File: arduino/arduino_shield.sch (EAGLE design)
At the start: 14 parts, among them IC3 PCF8574T, IC4 PCF8574T

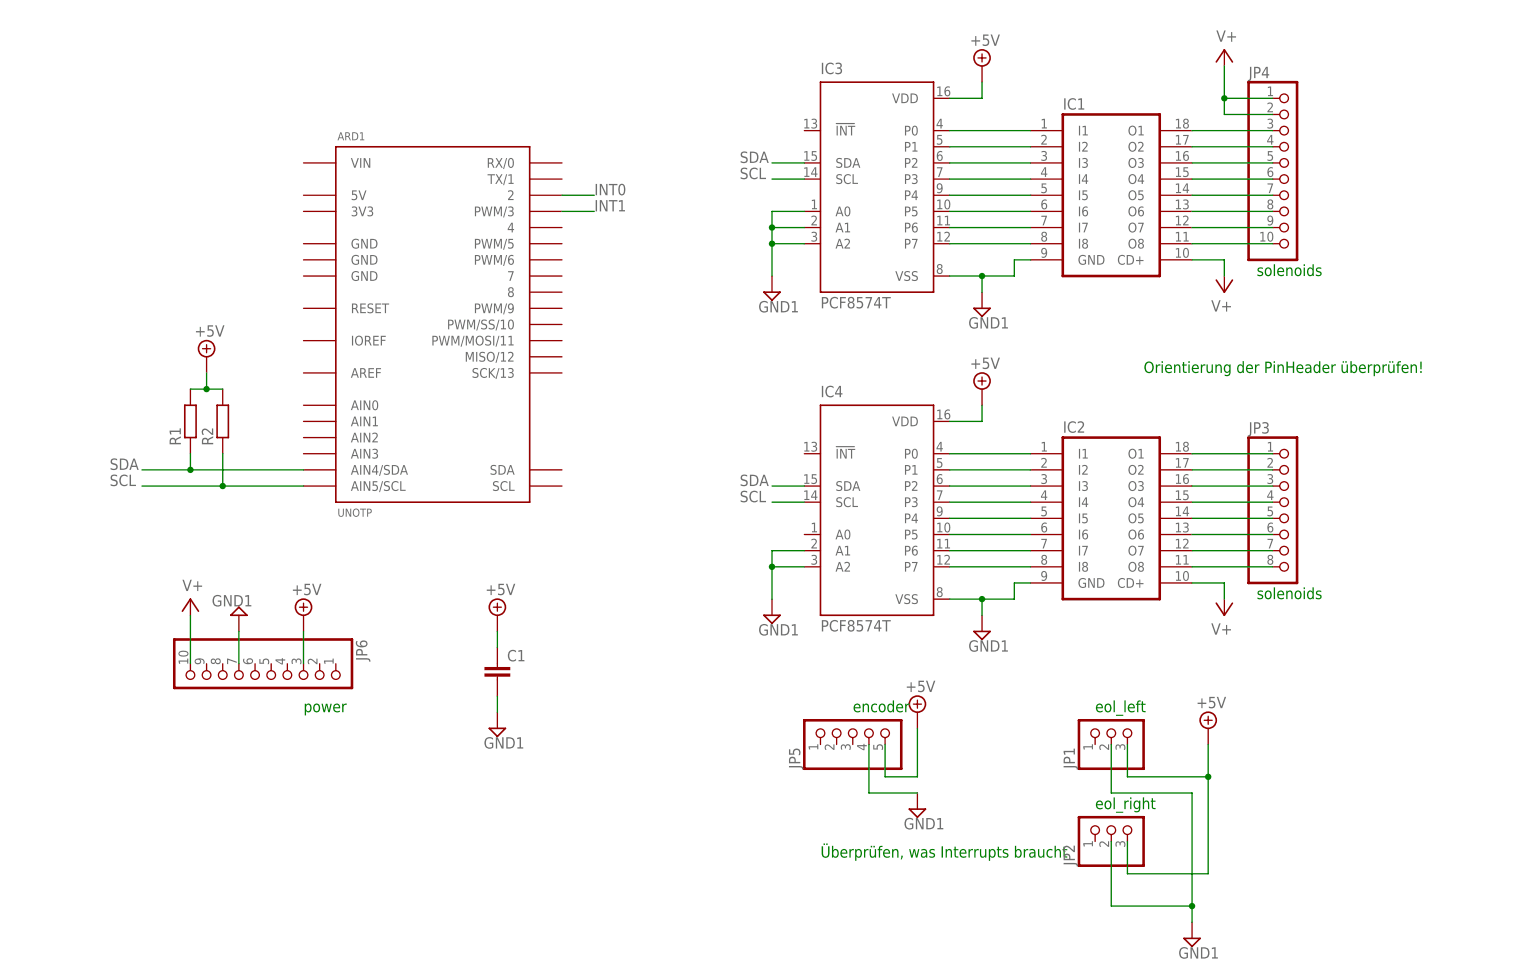
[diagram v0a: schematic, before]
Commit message: Wired EOLs and ENCODER to Arduino, added Buzzer and Supplyvoltage Jumper
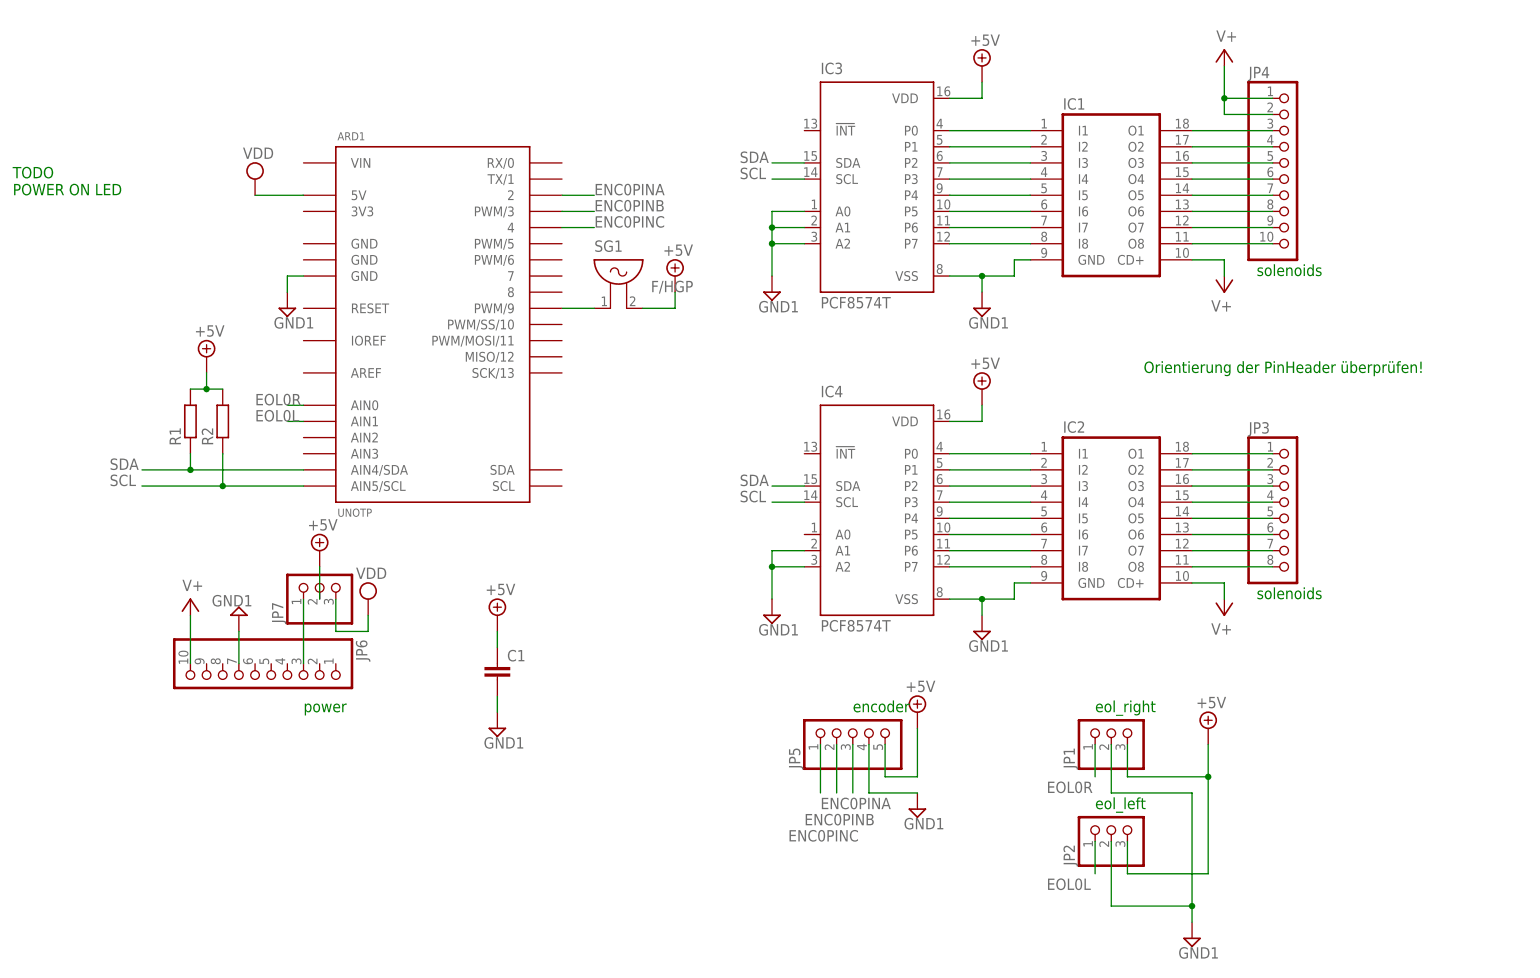
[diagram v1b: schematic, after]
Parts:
- added JP7: (no value), pinhead:PINHD-1X3
- added SG1: F/HGP, buzzer:F/HGP
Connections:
- removed net INT0: ARD1.2
- removed net INT1: ARD1.PWM/3
- new net ENC0PINA: ARD1.2, JP5.3
- new net ENC0PINB: ARD1.PWM/3, JP5.2
- new net ENC0PINC: ARD1.4, JP5.1
- new net EOL0L: ARD1.AIN1, JP2.1
- new net EOL0R: ARD1.AIN0, JP1.1
- new net N$33: JP6.3, JP7.1
- new net N$34: ARD1.PWM/9, SG1.1
- new net VDD: ARD1.5V, JP7.3
- net +5V: now also JP7.2, SG1.2; no longer JP6.3
- net GND1: now also ARD1.GND@3
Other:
- note added: "TODO POWER ON LED"
- note removed: "Überprüfen, was Interrupts braucht"
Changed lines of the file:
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@@
 <part name="SUPPLY13" library="supply2" deviceset="V+" device=""/>
 <part name="SUPPLY14" library="supply2" deviceset="GND1" device=""/>
-<part name="SUPPLY15" library="supply2" deviceset="+5V" device=""/>
 <part name="SUPPLY16" library="supply2" deviceset="+5V" device=""/>
 <part name="SUPPLY17" library="supply2" deviceset="GND1" device=""/>
 <part name="SUPPLY18" library="supply2" deviceset="GND1" device=""/>
 <part name="SUPPLY19" library="supply2" deviceset="+5V" device=""/>
+<part name="SUPPLY20" library="supply2" deviceset="GND1" device=""/>
+<part name="SG1" library="buzzer" deviceset="F/HGP" device=""/>
+<part name="SUPPLY21" library="supply2" deviceset="+5V" device=""/>
+<part name="JP7" library="pinhead" deviceset="PINHD-1X3" device=""/>
+<part name="SUPPLY15" library="supply2" deviceset="+5V" device=""/>
+<part name="SUPPLY22" library="supply2" deviceset="VDD" device=""/>
+<part name="SUPPLY23" library="supply2" deviceset="VDD" device=""/>
 </parts>
 <sheets>
 <sheet>
 <plain>
-<text x="25.4" y="-35.56" size="1.778" layer="91">eol_left</text>
-<text x="25.4" y="-50.8" size="1.778" layer="91">eol_right</text>
+<text x="25.4" y="-50.8" size="1.778" layer="91">eol_left</text>
+<text x="25.4" y="-35.56" size="1.778" layer="91">eol_right</text>
 <text x="-12.7" y="-35.56" size="1.778" layer="91">encoder</text>
 <text x="50.8" y="33.02" size="1.778" layer="91">solenoids</text>
@@
 <text x="-99.06" y="-35.56" size="1.778" layer="91">power</text>
 <text x="33.02" y="17.78" size="1.778" layer="91">Orientierung der PinHeader überprüfen!</text>
-<text x="-17.78" y="-58.42" size="1.778" layer="91">Überprüfen, was Interrupts braucht</text>
+<text x="-144.78" y="45.72" size="1.778" layer="91">TODO
+POWER ON LED</text>
 </plain>
 <instances>
@@
 <instance part="SUPPLY13" gate="1" x="-116.84" y="-17.78"/>
 <instance part="SUPPLY14" gate="G$1" x="-109.22" y="-20.32" rot="R180"/>
-<instance part="SUPPLY15" gate="+5V" x="-99.06" y="-20.32"/>
 <instance part="SUPPLY16" gate="+5V" x="43.18" y="-38.1"/>
 <instance part="SUPPLY17" gate="G$1" x="40.64" y="-71.12"/>
 <instance part="SUPPLY18" gate="G$1" x="-2.54" y="-50.8"/>
 <instance part="SUPPLY19" gate="+5V" x="-2.54" y="-35.56"/>
+<instance part="SUPPLY20" gate="G$1" x="-101.6" y="27.94"/>
+<instance part="SG1" gate="G$1" x="-50.8" y="30.48"/>
+<instance part="SUPPLY21" gate="+5V" x="-40.64" y="33.02"/>
+<instance part="JP7" gate="A" x="-96.52" y="-15.24" rot="R90"/>
+<instance part="SUPPLY15" gate="+5V" x="-96.52" y="-10.16"/>
+<instance part="SUPPLY22" gate="G$1" x="-106.68" y="48.26"/>
+<instance part="SUPPLY23" gate="G$1" x="-88.9" y="-17.78"/>
 </instances>
 <busses>
@@
 <wire x1="2.54" y1="10.16" x2="7.62" y2="10.16" width="0.1524" layer="91"/>
 <wire x1="7.62" y1="10.16" x2="7.62" y2="12.7" width="0.1524" layer="91"/>
-</segment>
-<segment>
-<pinref part="JP6" gate="A" pin="3"/>
-<pinref part="SUPPLY15" gate="+5V" pin="+5V"/>
-<wire x1="-99.06" y1="-27.94" x2="-99.06" y2="-22.86" width="0.1524" layer="91"/>
 </segment>
 <segment>
@@
 <wire x1="-7.62" y1="-45.72" x2="-2.54" y2="-45.72" width="0.1524" layer="91"/>
 <wire x1="-2.54" y1="-45.72" x2="-2.54" y2="-38.1" width="0.1524" layer="91"/>
+</segment>
+<segment>
+<pinref part="SG1" gate="G$1" pin="2"/>
+<wire x1="-45.72" y1="27.94" x2="-40.64" y2="27.94" width="0.1524" layer="91"/>
+<wire x1="-40.64" y1="27.94" x2="-40.64" y2="30.48" width="0.1524" layer="91"/>
+<pinref part="SUPPLY21" gate="+5V" pin="+5V"/>
+</segment>
+<segment>
+<pinref part="JP7" gate="A" pin="2"/>
+<pinref part="SUPPLY15" gate="+5V" pin="+5V"/>
+<wire x1="-96.52" y1="-17.78" x2="-96.52" y2="-12.7" width="0.1524" layer="91"/>
 </segment>
 </net>
@@
 <wire x1="-10.16" y1="-48.26" x2="-2.54" y2="-48.26" width="0.1524" layer="91"/>
 </segment>
+<segment>
+<pinref part="ARD1" gate="G$1" pin="GND@3"/>
+<wire x1="-99.06" y1="33.02" x2="-101.6" y2="33.02" width="0.1524" layer="91"/>
+<wire x1="-101.6" y1="33.02" x2="-101.6" y2="30.48" width="0.1524" layer="91"/>
+<pinref part="SUPPLY20" gate="G$1" pin="GND1"/>
+</segment>
 </net>
 <net name="N$2" class="0">
@@
 <junction x="-111.76" y="0"/>
 <label x="-129.54" y="0" size="1.778" layer="95"/>
-</segment>
-</net>
-<net name="INT0" class="0">
-<segment>
-<pinref part="ARD1" gate="G$1" pin="2"/>
-<wire x1="-58.42" y1="45.72" x2="-53.34" y2="45.72" width="0.1524" layer="91"/>
-<label x="-53.34" y="45.72" size="1.778" layer="95"/>
-</segment>
-</net>
-<net name="INT1" class="0">
-<segment>
-<pinref part="ARD1" gate="G$1" pin="PWM/3"/>
-<wire x1="-58.42" y1="43.18" x2="-53.34" y2="43.18" width="0.1524" layer="91"/>
-<label x="-53.34" y="43.18" size="1.778" layer="95"/>
 </segment>
 </net>
@@
 </segment>
 </net>
+<net name="ENC0PINA" class="0">
+<segment>
+<pinref part="JP5" gate="A" pin="3"/>
+<wire x1="-12.7" y1="-40.64" x2="-12.7" y2="-48.26" width="0.1524" layer="91"/>
+<label x="-17.78" y="-50.8" size="1.778" layer="95"/>
+</segment>
+<segment>
+<pinref part="ARD1" gate="G$1" pin="2"/>
+<wire x1="-58.42" y1="45.72" x2="-53.34" y2="45.72" width="0.1524" layer="91"/>
+<label x="-53.34" y="45.72" size="1.778" layer="95"/>
+</segment>
+</net>
+<net name="ENC0PINB" class="0">
+<segment>
+<pinref part="JP5" gate="A" pin="2"/>
+<wire x1="-15.24" y1="-40.64" x2="-15.24" y2="-48.26" width="0.1524" layer="91"/>
+<label x="-20.32" y="-53.34" size="1.778" layer="95"/>
+</segment>
+<segment>
+<pinref part="ARD1" gate="G$1" pin="PWM/3"/>
+<wire x1="-58.42" y1="43.18" x2="-53.34" y2="43.18" width="0.1524" layer="91"/>
+<label x="-53.34" y="43.18" size="1.778" layer="95"/>
+</segment>
+</net>
+<net name="ENC0PINC" class="0">
+<segment>
+<pinref part="JP5" gate="A" pin="1"/>
+<wire x1="-17.78" y1="-40.64" x2="-17.78" y2="-48.26" width="0.1524" layer="91"/>
+<label x="-22.86" y="-55.88" size="1.778" layer="95"/>
+</segment>
+<segment>
+<pinref part="ARD1" gate="G$1" pin="4"/>
+<wire x1="-58.42" y1="40.64" x2="-53.34" y2="40.64" width="0.1524" layer="91"/>
+<label x="-53.34" y="40.64" size="1.778" layer="95"/>
+</segment>
+</net>
+<net name="EOL0R" class="0">
+<segment>
+<pinref part="JP1" gate="A" pin="1"/>
+<wire x1="25.4" y1="-40.64" x2="25.4" y2="-45.72" width="0.1524" layer="91"/>
+<label x="17.78" y="-48.26" size="1.778" layer="95"/>
+</segment>
+<segment>
+<pinref part="ARD1" gate="G$1" pin="AIN0"/>
+<wire x1="-99.06" y1="12.7" x2="-101.6" y2="12.7" width="0.1524" layer="91"/>
+<label x="-106.68" y="12.7" size="1.778" layer="95"/>
+</segment>
+</net>
+<net name="EOL0L" class="0">
+<segment>
+<pinref part="JP2" gate="A" pin="1"/>
+<wire x1="25.4" y1="-55.88" x2="25.4" y2="-60.96" width="0.1524" layer="91"/>
+<label x="17.78" y="-63.5" size="1.778" layer="95"/>
+</segment>
+<segment>
+<pinref part="ARD1" gate="G$1" pin="AIN1"/>
+<wire x1="-99.06" y1="10.16" x2="-101.6" y2="10.16" width="0.1524" layer="91"/>
+<label x="-106.68" y="10.16" size="1.778" layer="95"/>
+</segment>
+</net>
+<net name="N$34" class="0">
+<segment>
+<pinref part="ARD1" gate="G$1" pin="PWM/9"/>
+<pinref part="SG1" gate="G$1" pin="1"/>
+<wire x1="-58.42" y1="27.94" x2="-53.34" y2="27.94" width="0.1524" layer="91"/>
+</segment>
+</net>
+<net name="N$33" class="0">
+<segment>
+<pinref part="JP6" gate="A" pin="3"/>
+<pinref part="JP7" gate="A" pin="1"/>
+<wire x1="-99.06" y1="-27.94" x2="-99.06" y2="-17.78" width="0.1524" layer="91"/>
+</segment>
+</net>
+<net name="VDD" class="0">
+<segment>
+<pinref part="ARD1" gate="G$1" pin="5V"/>
+<pinref part="SUPPLY22" gate="G$1" pin="VDD"/>
+<wire x1="-99.06" y1="45.72" x2="-106.68" y2="45.72" width="0.1524" layer="91"/>
+</segment>
+<segment>
+<pinref part="JP7" gate="A" pin="3"/>
+<wire x1="-93.98" y1="-17.78" x2="-93.98" y2="-22.86" width="0.1524" layer="91"/>
+<pinref part="SUPPLY23" gate="G$1" pin="VDD"/>
+<wire x1="-93.98" y1="-22.86" x2="-88.9" y2="-22.86" width="0.1524" layer="91"/>
+<wire x1="-88.9" y1="-22.86" x2="-88.9" y2="-20.32" width="0.1524" layer="91"/>
+</segment>
+</net>
 </nets>
 </sheet>
@@
 </schematic>
 </drawing>
+<compatibility>
+<note version="6.3" minversion="6.2.2" severity="warning">
+Since Version 6.2.2 text objects can contain more than one line,
+which will not be processed correctly with this version.
+</note>
+</compatibility>
 </eagle>

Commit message: Schematic an tatsaechliche Steckerbelegungen angepasst
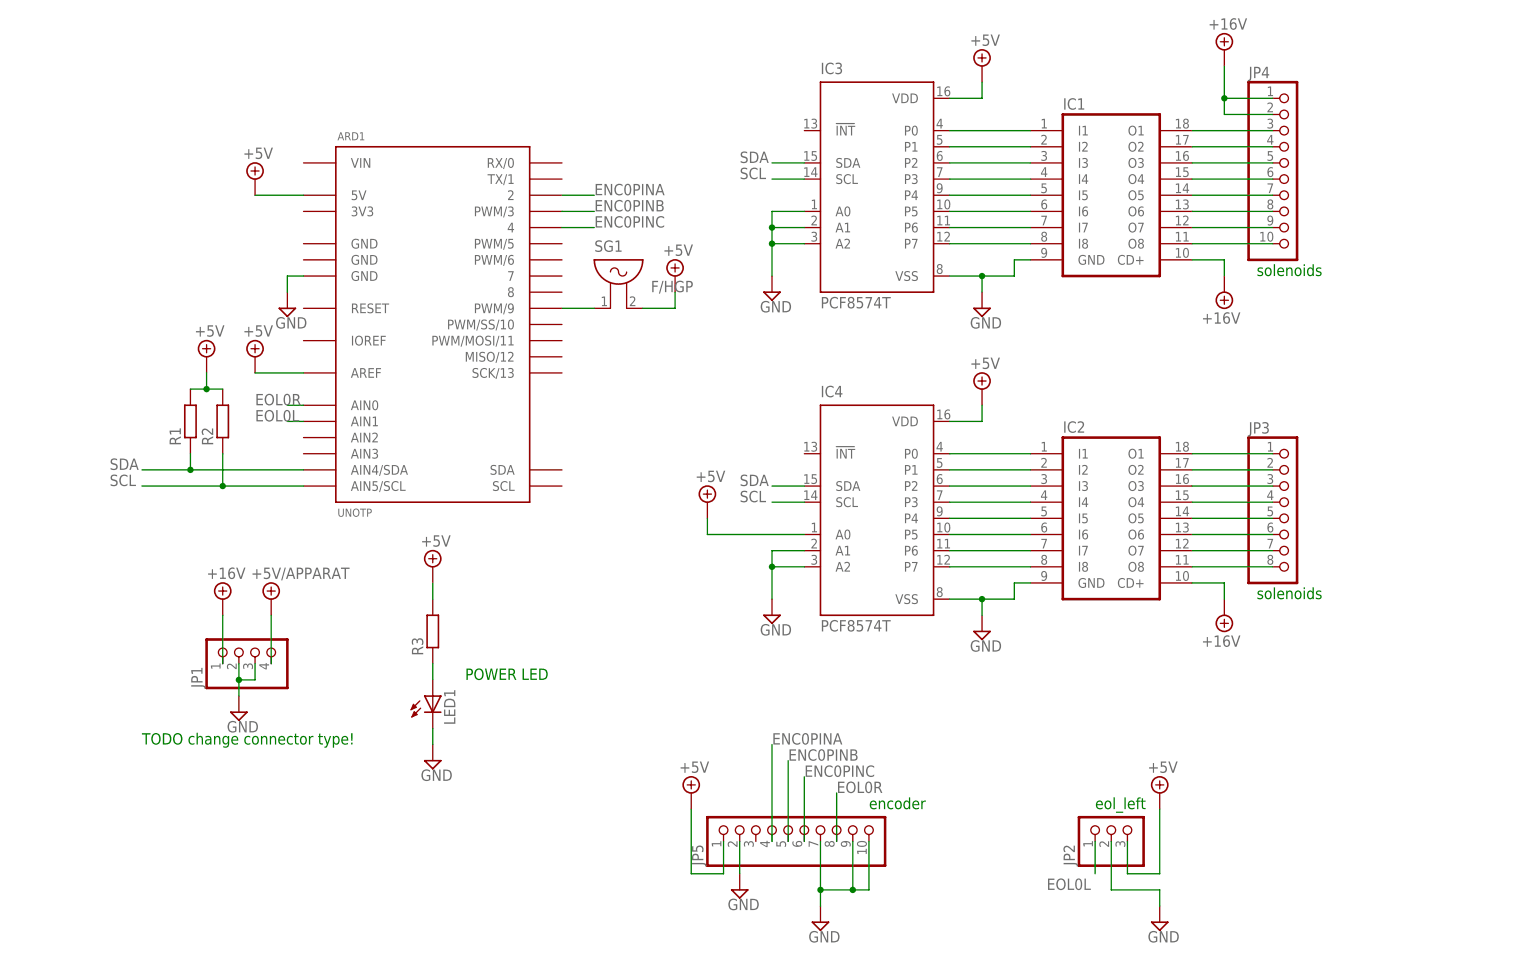
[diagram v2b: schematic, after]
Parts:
- removed C1: (no value), rcl:C-EUC0805
- removed JP6: (no value), pinheader_250:PINHD-1X10
- removed JP7: (no value), pinhead:PINHD-1X3
- added LED1: (no value), adafruit:LEDCHIP-LED0805
- added R3: (no value), resistor:R-EU_R0805
- JP1: device pinheader_250:PINHD-1X3 -> pinhead:PINHD-1X4
- JP5: device pinheader_250:PINHD-1X5 -> pinheader_250:PINHD-1X10
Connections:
- removed net GND1: ARD1.GND@3, C1.2, IC1.GND, IC2.GND, IC3.A0, IC3.A1, IC3.A2, IC3.VSS, IC4.A1, IC4.A2, IC4.VSS, JP1.2, JP2.2, JP5.4, JP6.7
- removed net V+: IC1.CD+, IC2.CD+, JP4.1, JP4.2, JP6.10
- removed net VDD: ARD1.5V, JP7.3
- new net +15V: IC1.CD+, IC2.CD+, JP4.1, JP4.2
- new net +16V: JP1.1
- new net +5V/APPARAT: JP1.4
- new net GND: ARD1.GND@3, IC1.GND, IC2.GND, IC3.A0, IC3.A1, IC3.A2, IC3.VSS, IC4.A1, IC4.A2, IC4.VSS, JP1.2, JP1.3, JP2.2, JP5.10, JP5.2, JP5.7, JP5.9, LED1.C
- net +5V: now also ARD1.5V, ARD1.AREF, IC4.A0, JP5.1, R3.2; no longer C1.1, JP1.3, JP5.5, JP7.2
- net ENC0PINA: now also JP5.4; no longer JP5.3
- net ENC0PINB: now also JP5.5; no longer JP5.2
- net ENC0PINC: now also JP5.6; no longer JP5.1
- net EOL0R: now also JP5.8; no longer JP1.1
- net N$33: now also LED1.A, R3.1; no longer JP6.3, JP7.1
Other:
- note added: "POWER LED"
- note added: "TODO change connector type!"
- note removed: "Orientierung der PinHeader überprüfen!"
- note removed: "TODO POWER ON LED"
- note removed: "eol_right"
- note removed: "power"

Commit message: Board erstellt
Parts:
- added LED2, LED3: (no value), adafruit:LEDCHIP-LED0805
- added R4, R5: (no value), resistor:R-EU_R0805
- JP1: value (none) -> POWERCON; device pinhead:PINHD-1X4 -> PowerCon:POWERCON
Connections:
- removed net +16V: JP1.1
- removed net +5V/APPARAT: JP1.4
- new net +5V/1: JP1.5V
- new net N$35: ARD1.PWM/6, LED3.C
- new net N$36: ARD1.PWM/5, LED2.C
- new net N$37: LED3.A, R4.2
- new net N$38: LED2.A, R5.2
- net +15V: now also JP1.16V
- net +5V: now also R4.1, R5.1
- net GND: now also ARD1.GND@1, ARD1.GND@2, JP1.GND1, JP1.GND2; no longer JP1.2, JP1.3
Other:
- note removed: "TODO change connector type!"
- moved on the sheet: IC1, JP4, SG1
